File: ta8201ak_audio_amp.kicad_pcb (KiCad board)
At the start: 2 copper layers, 40.1 x 49.7 mm, 19 parts, among them J1 INPUT, J2 OUTPUT, J3 POWER, U1 TA8201AK

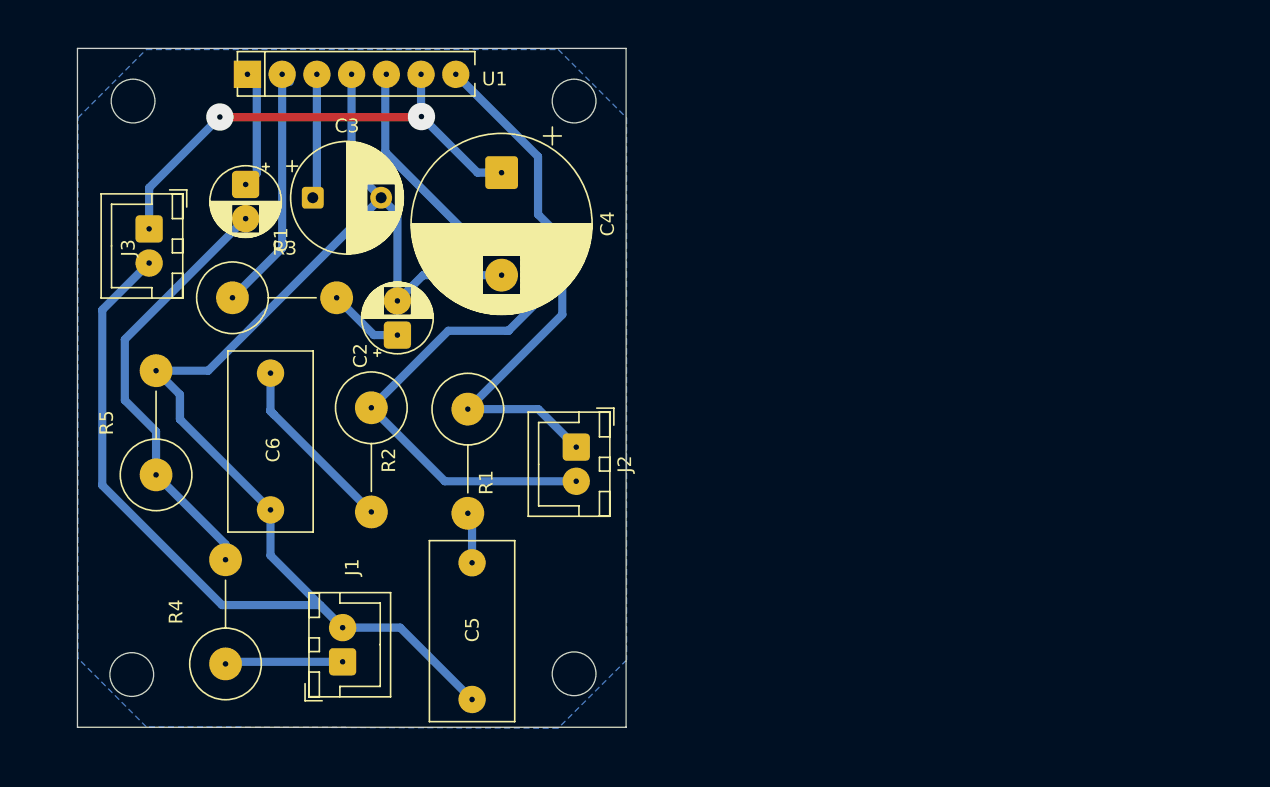
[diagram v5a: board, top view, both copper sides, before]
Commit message: 発振が酷いので部品配置を変更して解決できた 2.2Ω以外の抵抗は無くても利得が大きすぎるといったことは無いとおもう。
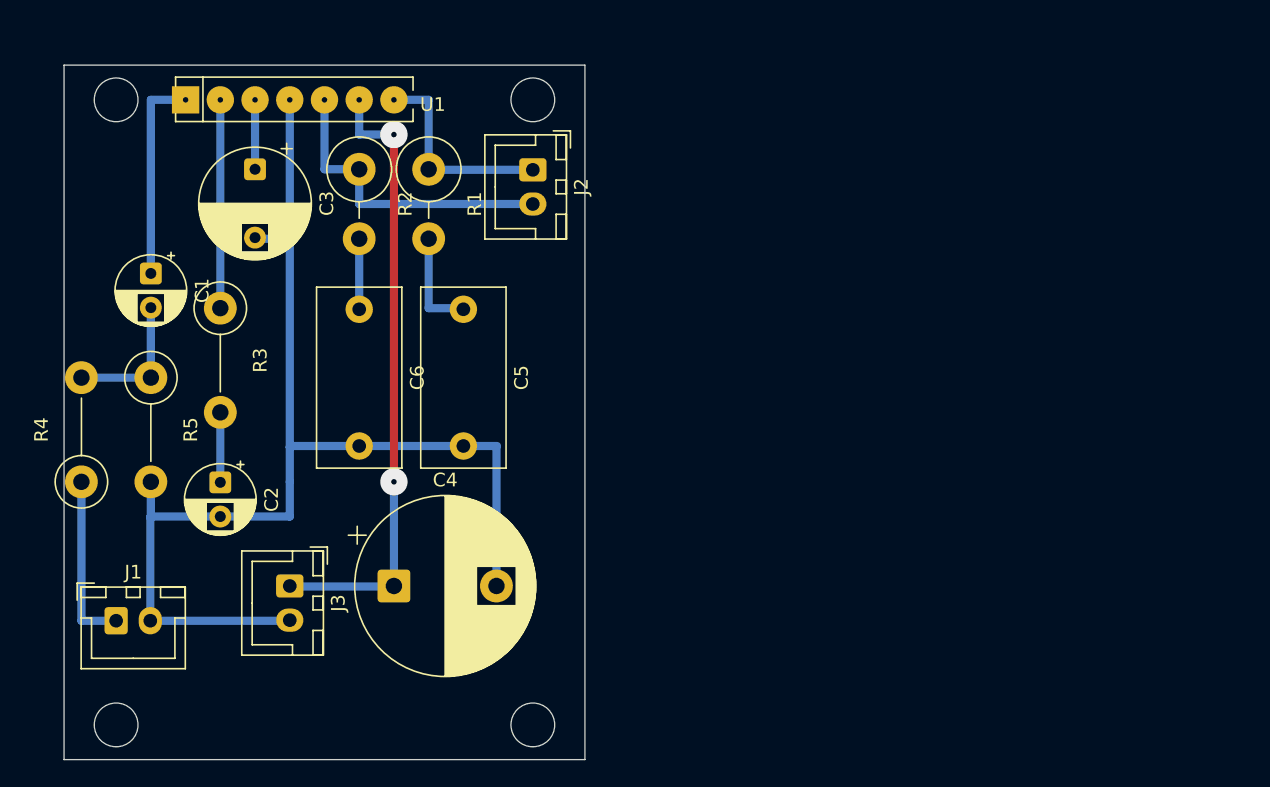
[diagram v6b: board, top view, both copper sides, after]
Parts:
- R1, R2: footprint Resistor_THT:R_Axial_DIN0516_L15.5mm_D5.0mm_P7.62mm_Vertical -> Resistor_THT:R_Axial_DIN0414_L11.9mm_D4.5mm_P5.08mm_Vertical
- R3, R4, R5: footprint Resistor_THT:R_Axial_DIN0516_L15.5mm_D5.0mm_P7.62mm_Vertical -> Resistor_THT:R_Axial_DIN0411_L9.9mm_D3.6mm_P7.62mm_Vertical
- moved C4 31.2 mm to (132.1, 86.4), turned to 0 degrees
- moved J3 28.1 mm to (124.5, 86.4)
- moved J2 20.5 mm to (142.2, 55.9)
- moved C5 18.6 mm to (137.2, 66.1)
- moved R1 17.8 mm to (134.6, 55.9)
- moved R2 17.5 mm to (129.5, 55.9)
- moved R4 17.0 mm to (109.2, 78.7)
- moved C2 16.8 mm to (119.4, 78.8), turned to -90 degrees
- moved J1 16.8 mm to (111.8, 88.9), turned to 0 degrees
- moved C1 9.51 mm to (114.3, 63.5)
- moved C6 7.99 mm to (129.5, 66.1)
- moved R5 7.12 mm to (114.3, 71.1), turned to -90 degrees
- moved U1 4.89 mm to (124.5, 50.7)
- moved H4 4.80 mm to (142.2, 96.5)
- moved C3 4.71 mm to (121.9, 55.9), turned to -90 degrees
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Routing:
- net GND: track 126.0 -> 88.8 mm
- net Net-(J2-Pin_2): track 56.7 -> 22.9 mm
- net Net-(J2-Pin_1): track 39.7 -> 15.3 mm
- net Net-(C1-Pad2): track 31.7 -> 10.2 mm
- net VCC: track 36.9 -> 45.8 mm
- net Net-(C6-Pad1): track 13.6 -> 5.16 mm
- net Net-(U1-IN): track 8.68 -> 15.2 mm
- net Net-(U1-R.F): track 9.58 -> 5.08 mm
- net Net-(J1-PadT): track 8.63 -> 12.7 mm
- net Net-(C5-Pad1): track 3.75 -> 7.65 mm
- net Net-(U1-NF): track 18.6 -> 15.2 mm
- removed copper zone on B.Cu, net (none)
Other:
- board size 40.1 x 49.7 mm -> 38.1 x 50.8 mm

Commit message: 発振が酷いので配置の見直しと配線を太くした
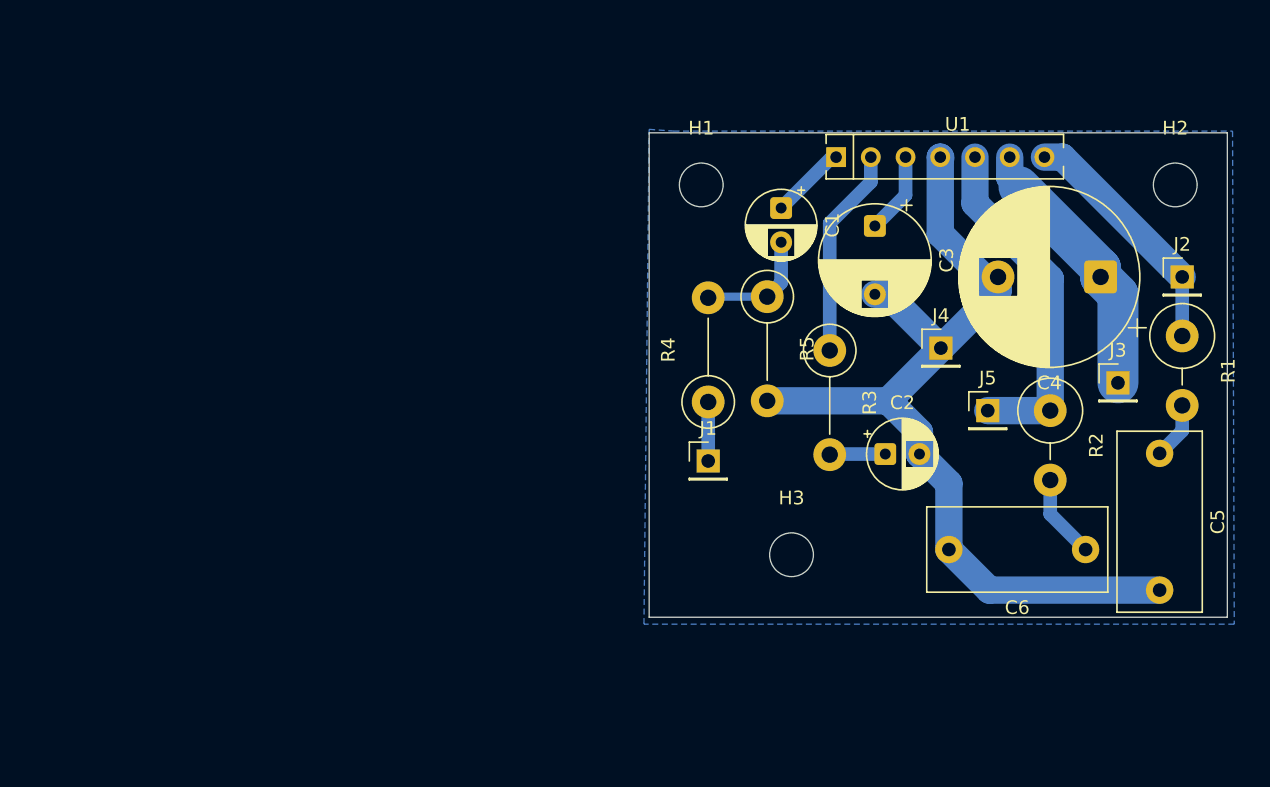
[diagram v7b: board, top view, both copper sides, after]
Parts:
- removed H4: MountingHole, MountingHole:MountingHole_3.2mm_M3
- added J4: Conn_01x01_Pin, Connector_PinHeader_2.54mm:PinHeader_1x01_P2.54mm_Vertical, F.Cu at (172.1, 69.0)
- added J5: Conn_01x01_Pin, Connector_PinHeader_2.54mm:PinHeader_1x01_P2.54mm_Vertical, F.Cu at (175.5, 73.5)
- J1: value INPUT -> Conn_01x01_Pin; footprint Connector_JST:JST_XH_B2B-XH-A_1x02_P2.50mm_Vertical -> Connector_PinHeader_2.54mm:PinHeader_1x01_P2.54mm_Vertical
- J2: value OUTPUT -> Conn_01x01_Pin; footprint Connector_JST:JST_XH_B2B-XH-A_1x02_P2.50mm_Vertical -> Connector_PinHeader_2.54mm:PinHeader_1x01_P2.54mm_Vertical
- J3: value POWER -> Conn_01x01_Pin; footprint Connector_JST:JST_XH_B2B-XH-A_1x02_P2.50mm_Vertical -> Connector_PinHeader_2.54mm:PinHeader_1x01_P2.54mm_Vertical
- R3: value 1.5k -> 620
- U1: footprint @MyLibrary:TA8201AK -> MyLibrary:TA8201AK
- moved J3 62.4 mm to (185.0, 71.5), turned to 0 degrees
- moved R1 56.5 mm to (189.7, 68.1)
- moved C4 56.4 mm to (183.8, 63.8), turned to 180 degrees
- moved C6 56.0 mm to (182.7, 83.7), turned to 180 degrees
- moved R2 53.5 mm to (180.1, 73.5)
- moved C5 52.0 mm to (188.1, 76.7)
- moved H3 50.9 mm to (161.2, 84.1)
- moved C2 48.7 mm to (168.0, 76.7), turned to 0 degrees
- moved J2 48.1 mm to (189.7, 63.8), turned to 0 degrees
- moved U1 47.8 mm to (172.1, 54.9)
- moved H2 47.4 mm to (189.2, 57.0)
- moved C1 46.3 mm to (160.4, 58.7)
- moved R4 46.2 mm to (155.1, 72.9)
- moved C3 45.5 mm to (167.3, 60.0)
- moved R5 45.5 mm to (159.4, 65.2)
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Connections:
- R2 pad 1: Net-(J2-Pin_2) -> Net-(J5-Pin_1)
- R4 pad 1: Net-(J1-PadT) -> Net-(J1-Pin_1)
- U1 pad 5: Net-(J2-Pin_2) -> Net-(J5-Pin_1)
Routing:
- net VCC: track 45.8 -> 19.8 mm, vias 2 -> 0
- net Net-(J5-Pin_1): track 0.00 -> 25.4 mm
- net Net-(J2-Pin_2): track 22.9 -> 0.00 mm
- net GND: track 88.8 -> 68.3 mm
- net Net-(J1-PadT): track 12.7 -> 0.00 mm
- net Net-(U1-IN): track 15.2 -> 5.56 mm
- net Net-(J1-Pin_1): track 0.00 -> 4.32 mm
- net Net-(C5-Pad1): track 7.65 -> 4.19 mm
- net Net-(J2-Pin_1): track 15.3 -> 18.0 mm
- net Net-(C1-Pad2): track 10.2 -> 8.87 mm
- net Net-(C2-Pad1): track 5.12 -> 4.08 mm
- net Net-(C6-Pad1): track 5.16 -> 6.15 mm
- net Net-(U1-R.F): track 5.08 -> 5.96 mm
- added copper zone on B.Cu, net GND
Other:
- board size 38.1 x 50.8 mm -> 42.3 x 35.4 mm

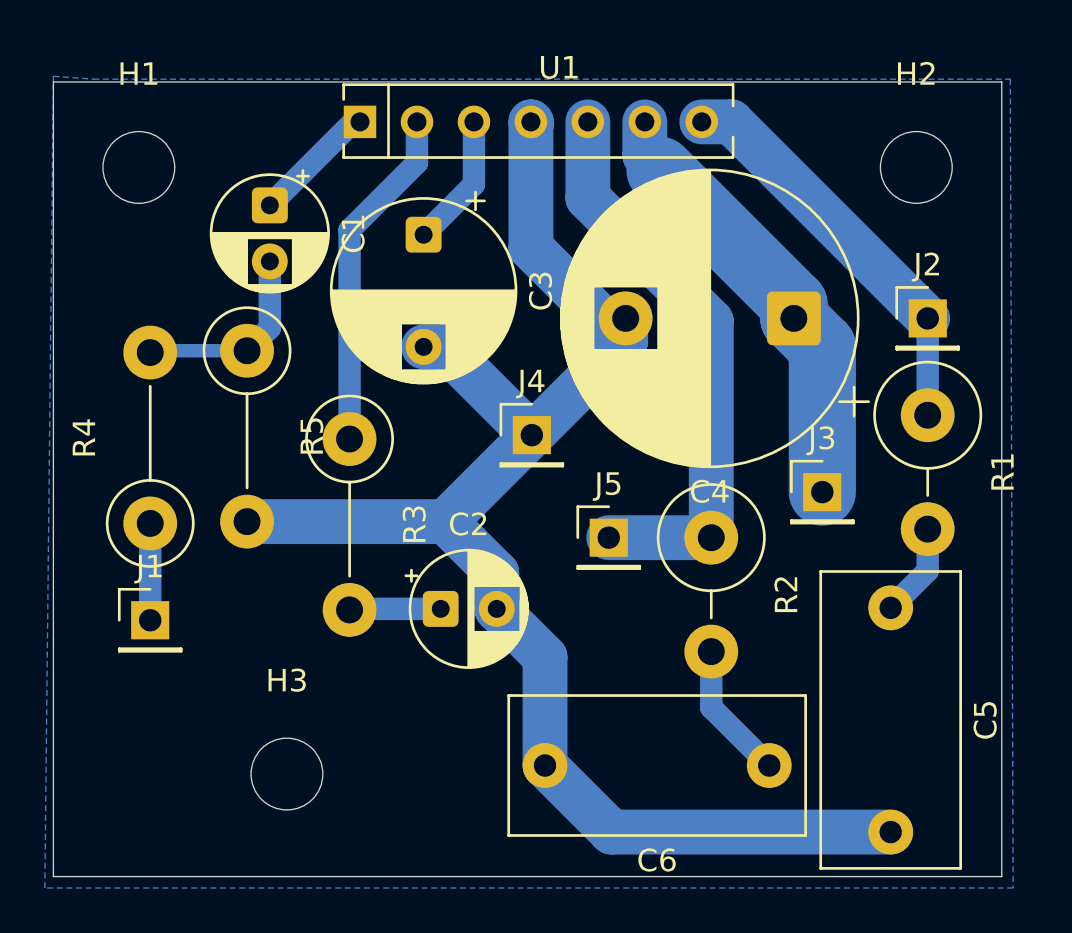
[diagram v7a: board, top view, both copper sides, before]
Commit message: ドリル穴が大きかったのを修正
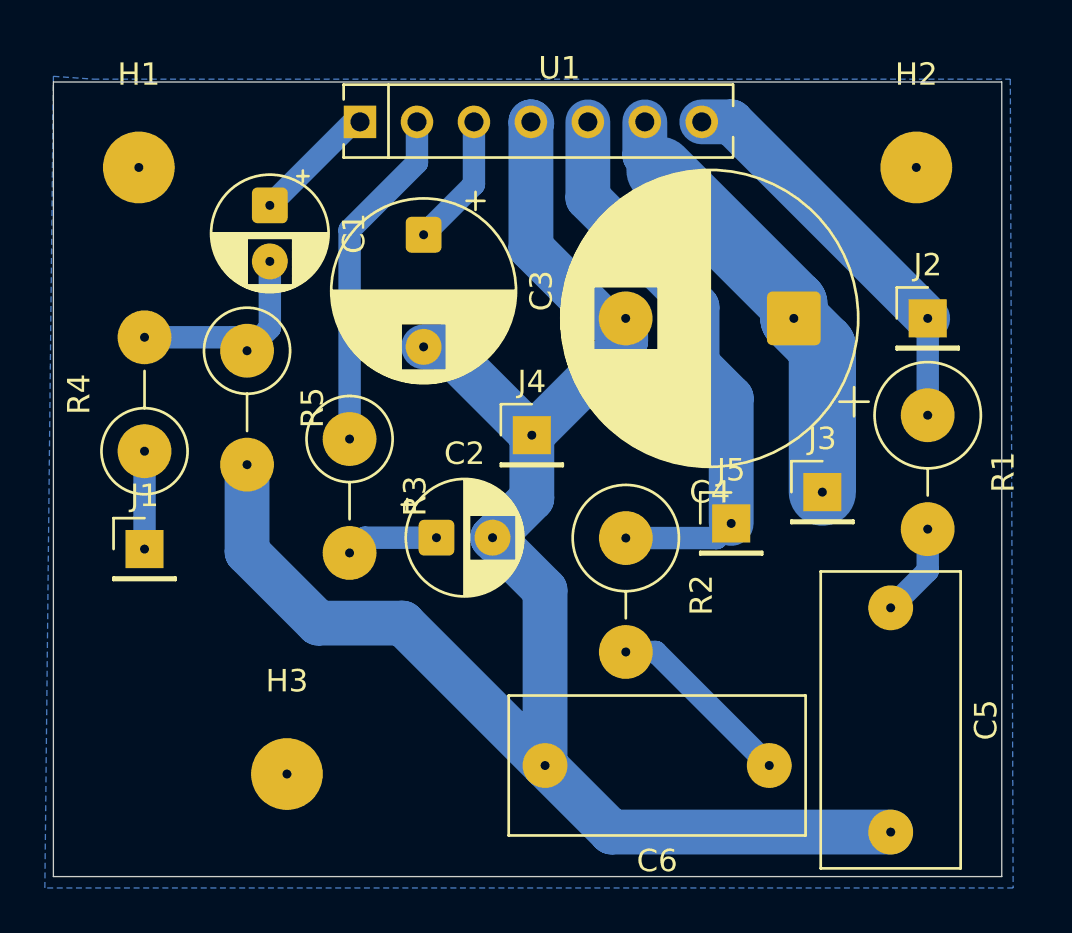
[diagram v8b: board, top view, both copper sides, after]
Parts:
- R3, R4, R5: footprint Resistor_THT:R_Axial_DIN0411_L9.9mm_D3.6mm_P7.62mm_Vertical -> Resistor_THT:R_Axial_DIN0411_L9.9mm_D3.6mm_P5.08mm_Vertical
- moved J5 5.50 mm to (181.0, 72.9)
- moved R2 3.81 mm to (176.3, 73.5)
- moved R4 3.23 mm to (154.8, 69.7)
- moved J1 3.19 mm to (154.8, 74.0)
- moved C2 3.18 mm to (167.8, 73.5)
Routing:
- net GND: track 68.3 -> 78.8 mm
- net Net-(C6-Pad1): track 6.15 -> 8.49 mm
